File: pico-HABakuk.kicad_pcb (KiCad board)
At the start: 2 copper layers, 52 x 51 mm, 59 parts, among them J1 USB_B_Micro, J2 Ant+, J4 Ant-, J5 Solar, J7 Super_Cap, SW1 USB BOOT, SW2 RESET, U1 NCP1117-3.3_SOT223, U2 W25Q128JVS, U3 RP2040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

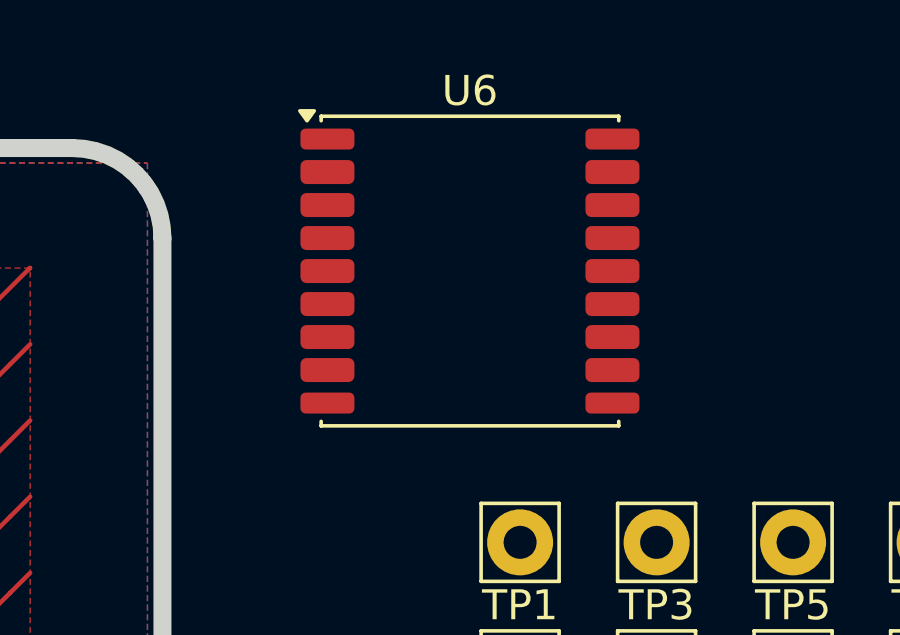
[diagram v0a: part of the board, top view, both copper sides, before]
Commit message: another GPS module 3D model
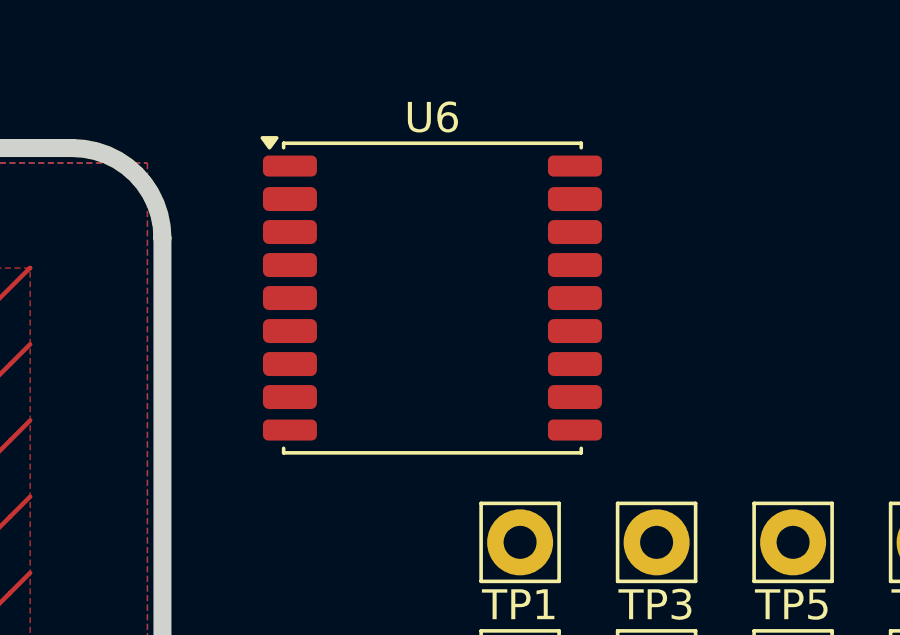
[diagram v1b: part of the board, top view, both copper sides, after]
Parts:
- moved U6 1.54 mm to (135.0, 75.0)
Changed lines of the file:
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@@
 	(footprint "RF_GPS:ublox_MAX"
 		(layer "F.Cu")
-		(at 136.25 74.1)
+		(at 135 75)
 		(descr "ublox MAX 6/7/8, (https://www.u-blox.com/sites/default/files/MAX-8-M8-FW3_HardwareIntegrationManual_%28UBX-15030059%29.pdf)")
 		(tags "GPS ublox MAX 6/7/8")
@@
 		)
 		(model "${KIPRJMOD}/MAX-8Q-0.STEP"
+			(hide yes)
 			(offset
 				(xyz 0 0 0)
+			)
+			(scale
+				(xyz 1 1 1)
+			)
+			(rotate
+				(xyz -90 0 0)
+			)
+		)
+		(model "${KIPRJMOD}/GP-02.stp"
+			(offset
+				(xyz 0 0 0)

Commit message: More work on schematics and PCB
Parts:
- added C25: 220uF, Capacitor_Tantalum_SMD:CP_EIA-3216-10_Kemet-I, F.Cu at (93.7, 118.5)
- added D3: BAT54W, Package_TO_SOT_SMD:SOT-323_SC-70, F.Cu at (94.7, 113.4)
- added J3: GPS Ant, Connector_PinSocket_2.54mm:PinSocket_1x02_P2.54mm_Vertical, F.Cu at (76.2, 109.8)
- added J6: Debug, Connector_PinHeader_2.54mm:PinHeader_1x03_P2.54mm_Vertical, F.Cu at (108.5, 72.0)
- added JP2: GPS+Glonass, Jumper:SolderJumper-2_P1.3mm_Bridged_RoundedPad1.0x1.5mm, F.Cu at (76.2, 113.6)
- added Q1: BSS84, Package_TO_SOT_SMD:SOT-23, F.Cu at (93.7, 107.1)
- added R12: 200, Resistor_SMD:R_0603_1608Metric, F.Cu at (109.2, 97.1)
- added R13: 100, Resistor_SMD:R_0603_1608Metric, F.Cu at (93.5, 99.4)
- added R14: 2k7, Resistor_SMD:R_0603_1608Metric, F.Cu at (105.4, 104.7)
- added R15: 3k9, Resistor_SMD:R_0603_1608Metric, F.Cu at (105.4, 108.0)
- added R2: 10k, Resistor_SMD:R_0603_1608Metric, F.Cu at (93.5, 103.0)
- added TP10: USB_D+, TestPoint:TestPoint_Pad_D1.5mm, F.Cu at (99.6, 88.2)
- added TP11: USB_D-, TestPoint:TestPoint_Pad_D1.5mm, F.Cu at (103.4, 88.2)
- added TP12: GND, TestPoint:TestPoint_Pad_D1.5mm, F.Cu at (111.0, 88.2)
- added TP13: USB_BOOT, TestPoint:TestPoint_Pad_D1.5mm, F.Cu at (95.8, 88.2)
- added TP14: Reset, TestPoint:TestPoint_Pad_D1.5mm, F.Cu at (91.9, 88.2)
- added TP15: SWCLK, TestPoint:TestPoint_Pad_D1.5mm, F.Cu at (107.2, 88.2)
- added TP16: SWD, TestPoint:TestPoint_Pad_D1.5mm, F.Cu at (114.8, 88.2)
- added TP9: +3V3, TestPoint:TestPoint_Pad_D1.5mm, F.Cu at (88.1, 88.2)
- C10, C11, C12, C13, C14, C15, C16, C2, C3, C5, C6, C7, C8, C9: footprint Capacitor_SMD:C_0402_1005Metric -> Capacitor_SMD:C_0603_1608Metric
- R1, R3, R4, R5: footprint Resistor_SMD:R_0402_1005Metric -> Resistor_SMD:R_0603_1608Metric
- TP1, TP2, TP3, TP4, TP5, TP6, TP7, TP8: footprint Connector_Pin:Pin_D1.1mm_L8.5mm_W2.5mm_FlatFork -> Connector_Pin:Pin_D1.1mm_L10.2mm_W3.5mm_Flat
- U6: value MAX-8Q -> GP-02
- moved J2 84.8 mm to (75.9, 99.9)
- moved SW1 74.3 mm to (78.7, 75.0), turned to 90 degrees
- moved U6 63.0 mm to (84.8, 113.1), turned to 180 degrees
- moved TP6 55.4 mm to (91.9, 81.4), turned to 90 degrees
- moved U5 52.3 mm to (108.7, 93.2), turned to 90 degrees
- moved TP5 51.3 mm to (95.8, 81.4), turned to 90 degrees
- moved TP1 49.8 mm to (88.1, 81.4), turned to 90 degrees
- moved C17 48.0 mm to (120.1, 110.8), turned to -90 degrees
- moved TP7 44.4 mm to (107.2, 81.4), turned to 90 degrees
- moved JP1 40.8 mm to (110.2, 101.1), turned to 90 degrees
- moved J5 40.4 mm to (111.2, 118.5), turned to -90 degrees
- moved TP3 39.1 mm to (103.4, 81.4), turned to 90 degrees
- moved TP2 38.8 mm to (99.6, 81.4), turned to 90 degrees
- moved J4 38.3 mm to (123.7, 99.9)
- moved D2 37.4 mm to (117.3, 98.4), turned to 180 degrees
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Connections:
- U6 pad 11: unconnected-(U6-RF_IN-Pad11) -> Net-(J3-Pin_1)
- U6 pad 13: unconnected-(U6-LNA_EN-Pad13) -> Net-(JP2-B)
- U6 pad 6: unconnected-(U6-V_BCKP-Pad6) -> Net-(D3-K)
- U6 pad 8: +3V3 -> Net-(Q1-S)
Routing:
- net +3V3: track 40.2 -> 100.7 mm
- net GND: track 29.7 -> 82.4 mm, vias 22 -> 0
- net /~{USB_BOOT}: track 5.34 -> 39.0 mm, vias 0 -> 1
- net /GPIO29_ADC3: track 33.2 -> 0.00 mm
- net /GPIO0: track 31.8 -> 0.00 mm
- net /GPIO28_ADC2: track 31.6 -> 0.00 mm
- net /GPIO27_ADC1: track 29.9 -> 0.00 mm
- net /GPIO26_ADC0: track 28.3 -> 0.00 mm
- net /GPIO3: track 26.9 -> 0.00 mm
- net /RUN: track 22.8 -> 49.5 mm, vias 0 -> 2
- net /GPIO15: track 25.4 -> 0.00 mm
- net /GPIO4: track 25.3 -> 0.00 mm
- net /GPIO24: track 25.0 -> 0.00 mm
- net Net-(J1-VBUS): track 2.11 -> 26.4 mm, vias 0 -> 2
- net /GPIO14: track 23.8 -> 0.00 mm
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- removed copper zone on B.Cu, net GND
- removed copper zone on F.Cu, net Net-(J1-VBUS)
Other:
- board size 52 x 51 mm -> 52 x 51.1 mm
- board text removed: "3V3"
- board text removed: "GP0"
- board text removed: "GP1"
- board text removed: "GP10"
- board text removed: "GP11"
- board text removed: "GP12"
- board text removed: "GP13"
- board text removed: "GP14"
- board text removed: "GP15"
- board text removed: "GP16"
- board text removed: "GP17"
- board text removed: "GP18"
- board text removed: "GP19"
- board text removed: "GP2"
- board text removed: "GP20"
- board text removed: "GP21"
- board text removed: "GP22"
- board text removed: "GP23"
- board text removed: "GP24"
- board text removed: "GP25"
- board text removed: "GP26"
- board text removed: "GP27"
- board text removed: "GP28"
- board text removed: "GP29"
- board text removed: "GP3"
- board text removed: "GP4"
- board text removed: "GP5"
- board text removed: "GP6"
- board text removed: "GP7"
- board text removed: "GP8"
- board text removed: "GP9"
- board text removed: "RUN"
- board text removed: "SWCLK"
- board text removed: "SWD"

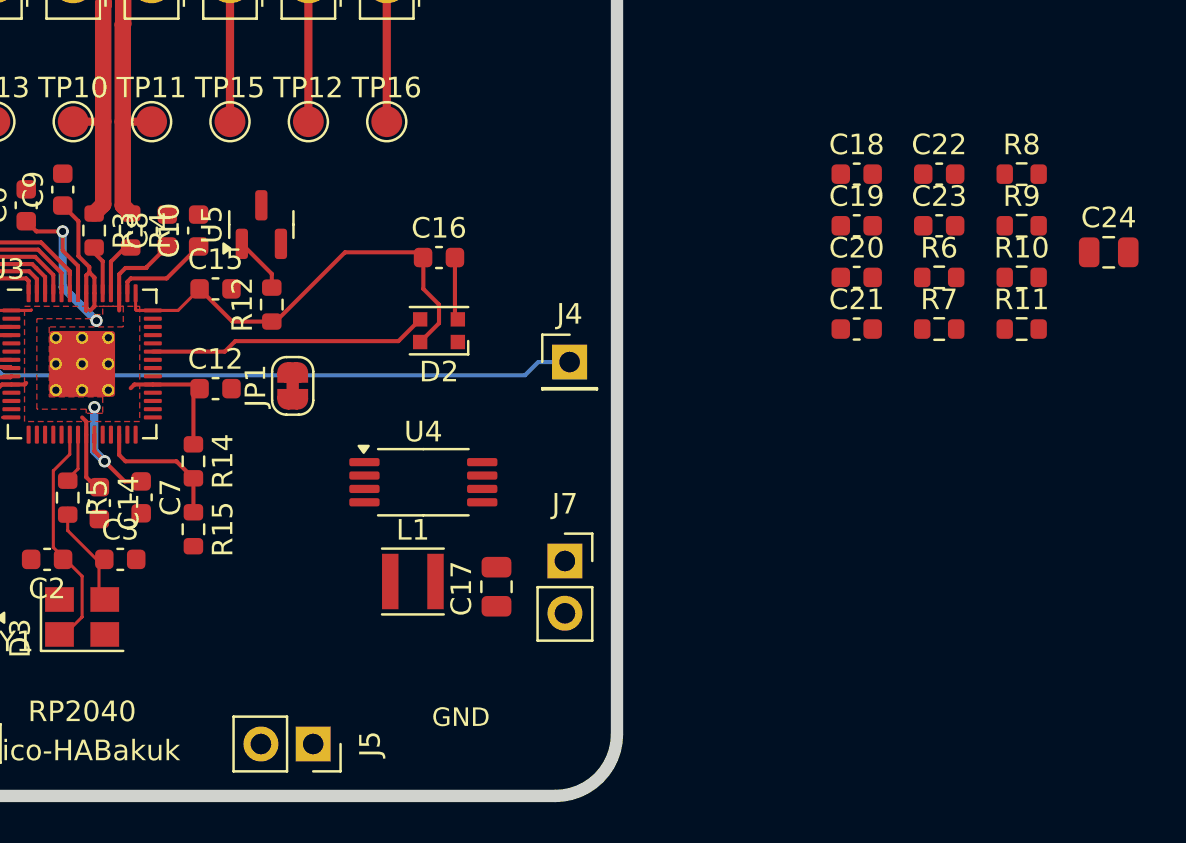
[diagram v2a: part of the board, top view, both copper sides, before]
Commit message: Max809 added
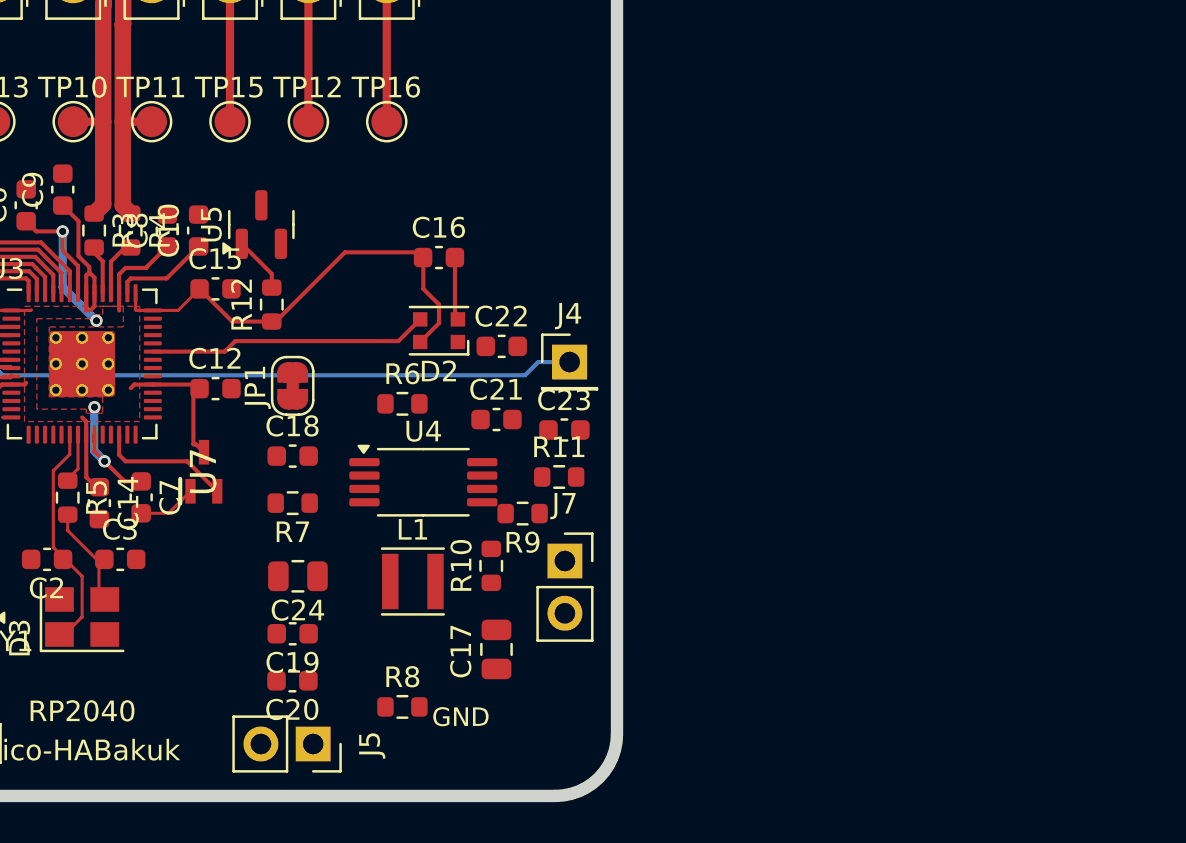
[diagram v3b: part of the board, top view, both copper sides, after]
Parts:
- removed R14: 2k7, Resistor_SMD:R_0603_1608Metric
- removed R15: 3k9, Resistor_SMD:R_0603_1608Metric
- added U7: MAX809STRG, SamacSys_Parts:SOT65P210X110-3N, F.Cu at (105.9, 105.2)
- moved C24 42.4 mm to (110.5, 110.3), turned to 180 degrees
- moved R8 39.7 mm to (115.6, 116.7)
- moved C19 33.8 mm to (110.2, 113.1), turned to 180 degrees
- moved C20 33.7 mm to (110.2, 115.4), turned to 180 degrees
- moved R7 32.5 mm to (110.2, 106.8), turned to 180 degrees
- moved C18 30.7 mm to (110.2, 104.5)
- moved R10 29.3 mm to (119.9, 109.8), turned to 90 degrees
- moved R9 28.0 mm to (121.4, 107.3), turned to 180 degrees
- moved R6 26.8 mm to (115.6, 101.9)
- moved R11 23.6 mm to (123.2, 105.5)
- moved C22 22.9 mm to (120.4, 99.1)
- moved C23 20.7 mm to (123.4, 103.2)
- moved C21 18.1 mm to (120.1, 102.7)
- moved C17 3.05 mm to (120.1, 113.9)
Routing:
- net GND: track 82.4 -> 85.3 mm
- net +3V3: track 100.7 -> 101.4 mm

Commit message: Work on PCB
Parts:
- added D1: SMM4F5.0A-TR, SamacSys_Parts:SMM4F15ATR, F.Cu at (117.5, 116.0)
- moved C22 10.0 mm to (124.0, 108.5), turned to -90 degrees
- moved R9 10.00 mm to (114.2, 114.2)
- moved C23 9.96 mm to (118.8, 112.0), turned to -90 degrees
- moved R8 9.27 mm to (122.0, 110.0), turned to -90 degrees
- moved R11 8.81 mm to (117.2, 112.0), turned to -90 degrees
- moved L1 8.01 mm to (108.4, 108.2)
- moved C18 7.72 mm to (108.5, 112.0)
- moved R7 7.00 mm to (114.2, 112.5), turned to 0 degrees
- moved R6 5.29 mm to (111.2, 105.0)
- moved C24 5.03 mm to (111.5, 115.2), turned to -90 degrees
- moved J7 4.93 mm to (123.8, 114.5)
- moved C21 4.14 mm to (121.0, 106.8)
- moved J5 4.01 mm to (107.2, 119.0), turned to 90 degrees
- moved U4 2.75 mm to (115.0, 108.0)
- moved C19 1.95 mm to (108.5, 114.0), turned to 0 degrees
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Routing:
- net +3V3: track 101.4 -> 164.6 mm, vias 2 -> 4
- net /RUN: track 49.3 -> 96.9 mm, vias 2 -> 4
- net GND: track 85.3 -> 126.8 mm, vias 0 -> 27
- net /SWD: track 16.8 -> 49.4 mm, vias 0 -> 2
- net /SWCLK: track 16.8 -> 43.3 mm, vias 0 -> 2
- net /Solar+: track 0.00 -> 20.0 mm
- net /GPIO28_ADC2: track 0.00 -> 13.1 mm, vias 0 -> 2
- net Net-(U4-ICTRL_PLUS): track 0.00 -> 13.0 mm
- net Net-(U4-MPPT-SET): track 0.00 -> 10.0 mm
- net Net-(U4-VOUT): track 0.00 -> 9.06 mm
- net Net-(U4-ICTRL_MINUS): track 0.00 -> 6.81 mm
- net Net-(U4-VCTRL): track 0.00 -> 6.17 mm
- net +1V1: track 21.0 -> 25.8 mm
- net Net-(U4-LX): track 0.00 -> 2.65 mm
- net Net-(U3-XOUT): track 2.76 -> 4.49 mm
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- added copper zone on B.Cu, net GND
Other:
- outline, holes or cut-outs redrawn

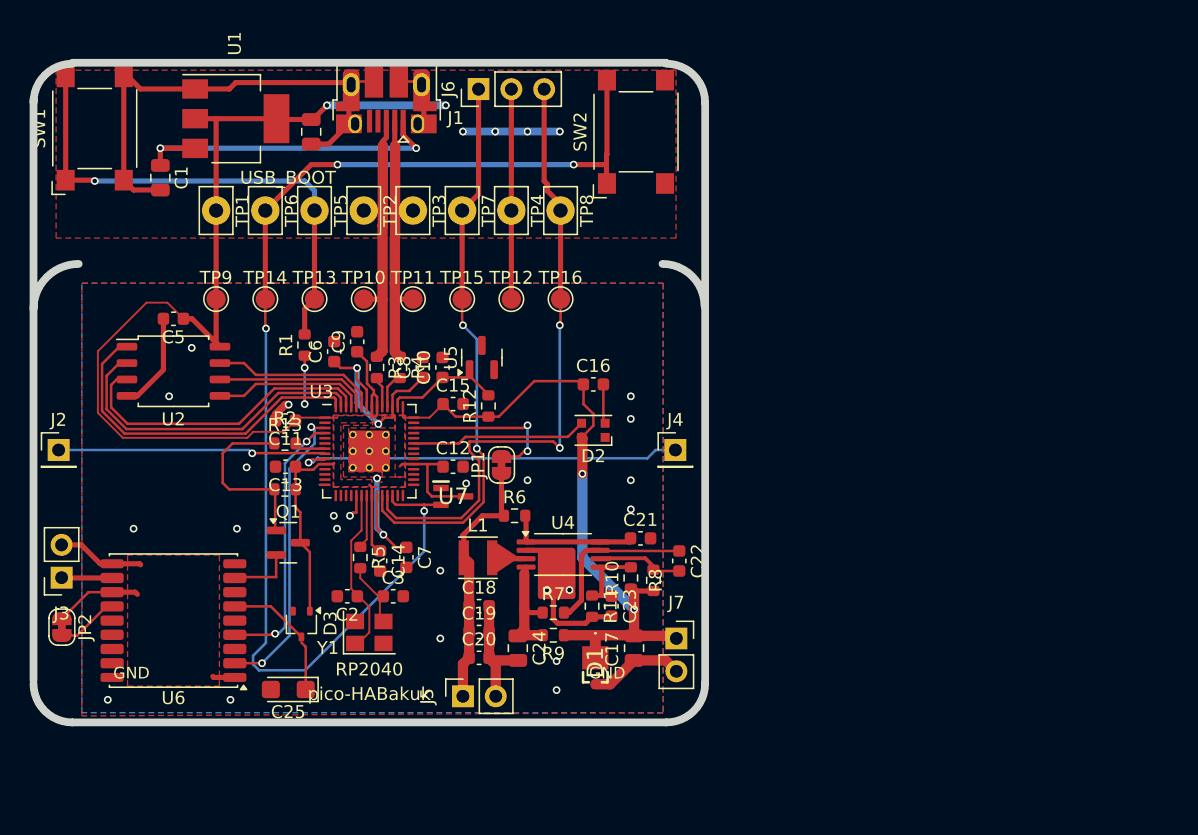
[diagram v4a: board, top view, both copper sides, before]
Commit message: board finetuning, GPIO pins added
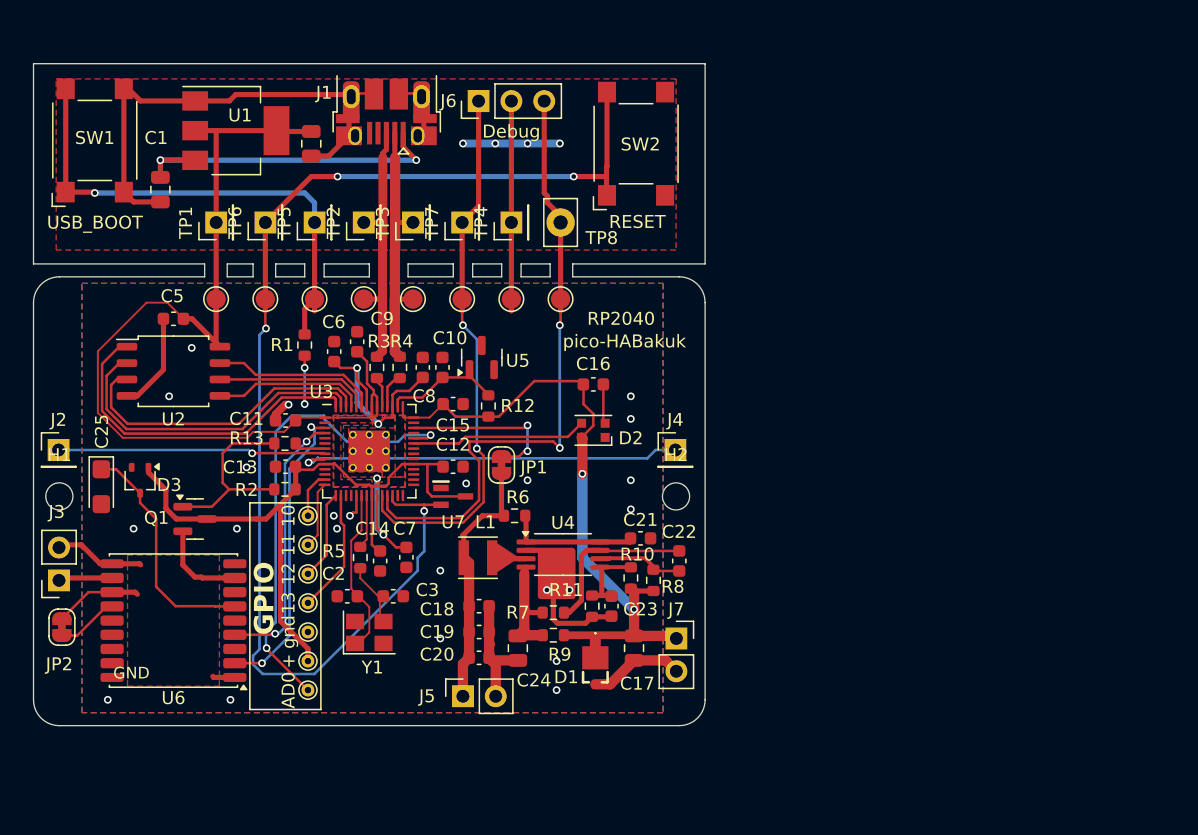
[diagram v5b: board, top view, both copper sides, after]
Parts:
- added H1: MountingHole, MountingHole:MountingHole_2.1mm, F.Cu at (76.0, 103.5)
- added H2: MountingHole, MountingHole:MountingHole_2.1mm, F.Cu at (123.8, 103.5)
- added TP17: 10, TestPoint:TestPoint_THTPad_D1.0mm_Drill0.5mm, F.Cu at (95.2, 105.0)
- added TP18: 11, TestPoint:TestPoint_THTPad_D1.0mm_Drill0.5mm, F.Cu at (95.2, 107.2)
- added TP19: 12, TestPoint:TestPoint_THTPad_D1.0mm_Drill0.5mm, F.Cu at (95.2, 109.5)
- added TP20: 13, TestPoint:TestPoint_THTPad_D1.0mm_Drill0.5mm, F.Cu at (95.2, 111.8)
- added TP21: gnd, TestPoint:TestPoint_THTPad_D1.0mm_Drill0.5mm, F.Cu at (95.2, 114.0)
- added TP22: +, TestPoint:TestPoint_THTPad_D1.0mm_Drill0.5mm, F.Cu at (95.2, 116.2)
- added TP23: AD0, TestPoint:TestPoint_THTPad_D1.0mm_Drill0.5mm, F.Cu at (95.2, 118.5)
- TP1, TP2, TP3, TP4, TP5, TP6, TP7: footprint Connector_Pin:Pin_D1.1mm_L10.2mm_W3.5mm_Flat -> Connector_PinHeader_2.54mm:PinHeader_1x01_P2.54mm_Vertical
- moved C25 21.4 mm to (79.2, 102.8), turned to -90 degrees
- moved D3 16.7 mm to (82.2, 102.2)
- moved Q1 7.46 mm to (86.5, 105.2)
- moved C1 0.93 mm to (83.8, 79.8)
- moved C4 0.93 mm to (95.5, 76.2)
- moved J1 0.93 mm to (101.3, 72.5)
- moved J6 0.93 mm to (108.5, 72.9)
- moved SW1 0.93 mm to (78.7, 75.9)
- moved SW2 0.93 mm to (120.7, 76.2)
- moved TP1 0.93 mm to (88.1, 82.3)
- moved TP2 0.93 mm to (99.6, 82.3)
- moved TP3 0.93 mm to (103.4, 82.3)
- moved TP4 0.93 mm to (111.0, 82.3)
- moved TP5 0.93 mm to (95.8, 82.3)
- moved TP6 0.93 mm to (92.0, 82.3)
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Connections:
- D1 pad 3: (no net) -> +3V3
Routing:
- net /GPIO26_ADC0: track 0.00 -> 36.8 mm, vias 0 -> 2
- net +3V3: track 164.6 -> 181.2 mm, vias 4 -> 2
- net /GPIO13: track 0.00 -> 9.58 mm
- net Net-(D3-K): track 9.91 -> 18.2 mm
- net /GPIO12: track 0.00 -> 6.95 mm
- net /GPIO11: track 0.43 -> 5.63 mm
- net /GPIO10: track 0.00 -> 3.63 mm
- net Net-(Q1-S): track 4.94 -> 7.15 mm
- net Net-(Q1-G): track 14.1 -> 15.1 mm
- net /RUN: track 96.9 -> 97.7 mm
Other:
- board size 52 x 51.1 mm -> 52 x 51.2 mm
- board text added: "+"
- board text added: "-"
- board text added: "Ant+"
- board text added: "Ant-"
- board text added: "Breakaway part"
- board text added: "Callsign:"
- board text added: "GPIO"
- board text added: "GPS Ant"
- board text added: "Launch date:"
- board text added: "Remarks:"
- board text added: "Rev. 1"
- board text added: "Solar"
- board text added: "Super cap"
- board text added: "e-Mail:"
- board text added: "github.com/serych/pico-HABakuk"

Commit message: Final board tuning and DRC debuging
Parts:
- added C26: 10u, Capacitor_SMD:C_0805_2012Metric, F.Cu at (117.5, 102.8)
- added C27: 10u, Capacitor_SMD:C_0805_2012Metric, F.Cu at (117.5, 104.8)
- added R14: 2k2, Resistor_SMD:R_0603_1608Metric, F.Cu at (104.5, 105.8)
- TP10: value USB_D+ -> D+
- TP11: value USB_D- -> D-
- TP12: value GND -> gnd
- TP13: value USB_BOOT -> boot
- TP14: value Reset -> rst
- TP15: value SWCLK -> swclk
- TP16: value SWD -> swd
- TP9: value +3V3 -> +
- moved C25 1.25 mm to (80.5, 102.8)
- moved D3 1.25 mm to (83.5, 102.2)
- moved C7 0.65 mm to (102.5, 108.8)
- moved H1 0.50 mm to (76.5, 103.5)
- moved H2 0.50 mm to (123.2, 103.5)
- moved Q1 0.50 mm to (87.0, 105.2)
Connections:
- U7 pad 2: /RUN -> Net-(U7-~{RESET})
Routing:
- net +3V3: track 181.2 -> 185.8 mm
- net /SWCLK: track 43.3 -> 45.9 mm
- net /SWD: track 49.4 -> 51.6 mm
- net GND: track 126.8 -> 128.6 mm
- net Net-(U7-~{RESET}): track 0.00 -> 1.19 mm
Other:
- board text removed: "GND"
